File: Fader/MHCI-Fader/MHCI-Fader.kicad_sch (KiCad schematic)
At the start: 29 parts, among them J1 Conn_01x06, SW1 SW_Push_LED, U1 TJA1051T, U3 SRV05-4

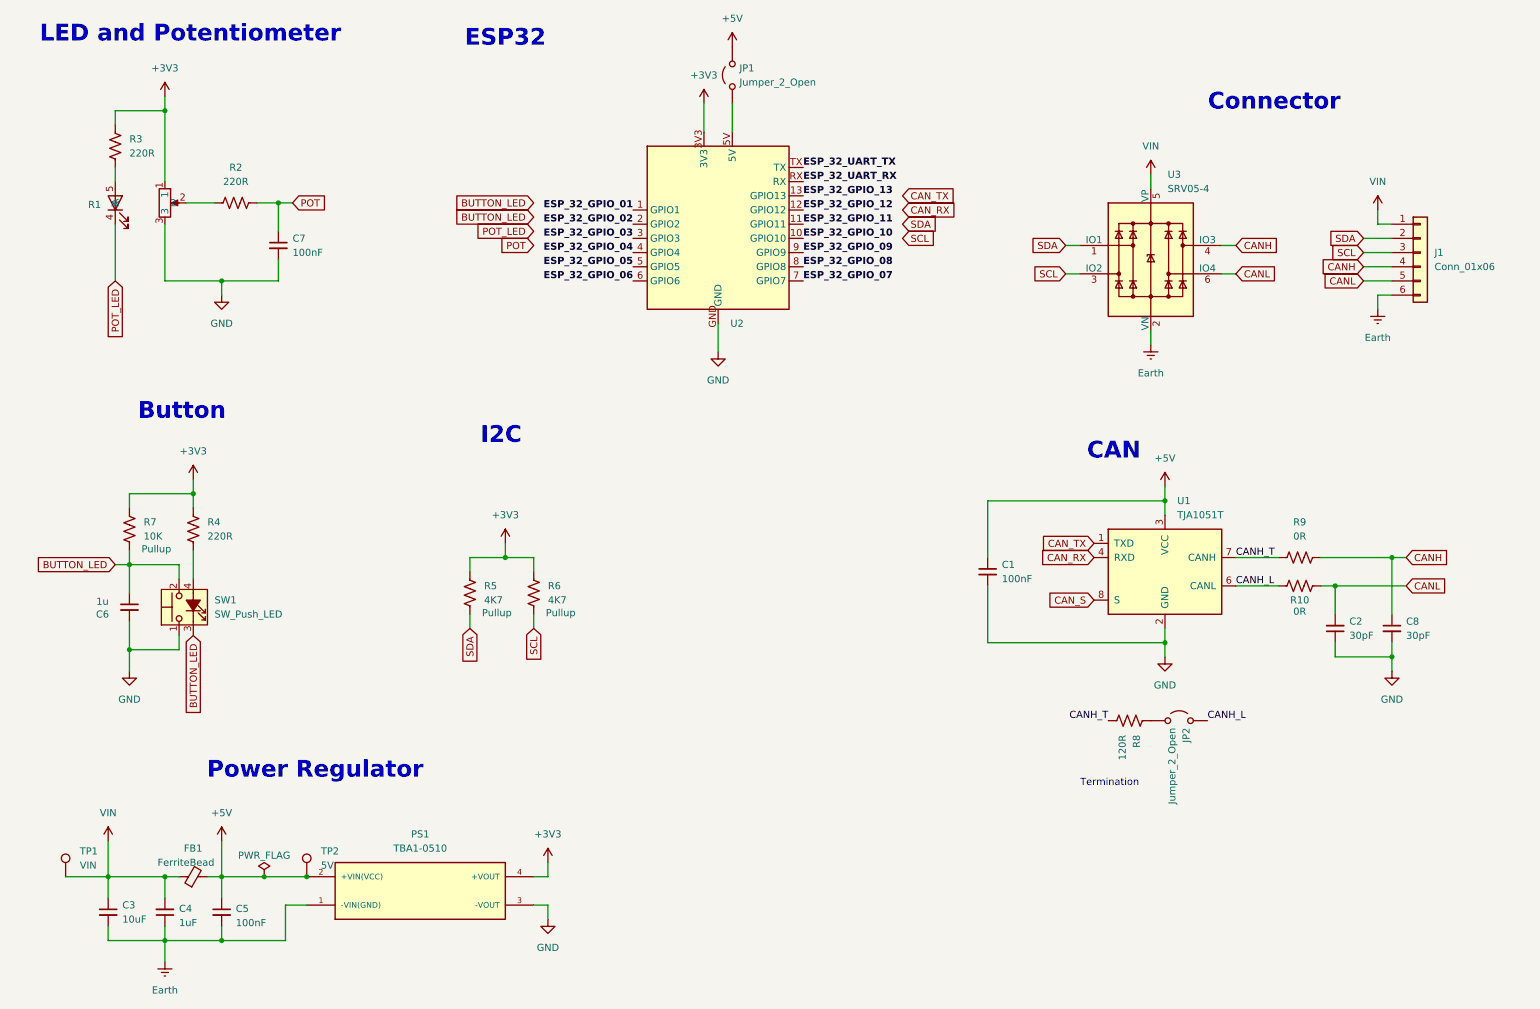
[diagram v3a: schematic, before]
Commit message: Fader layout complete
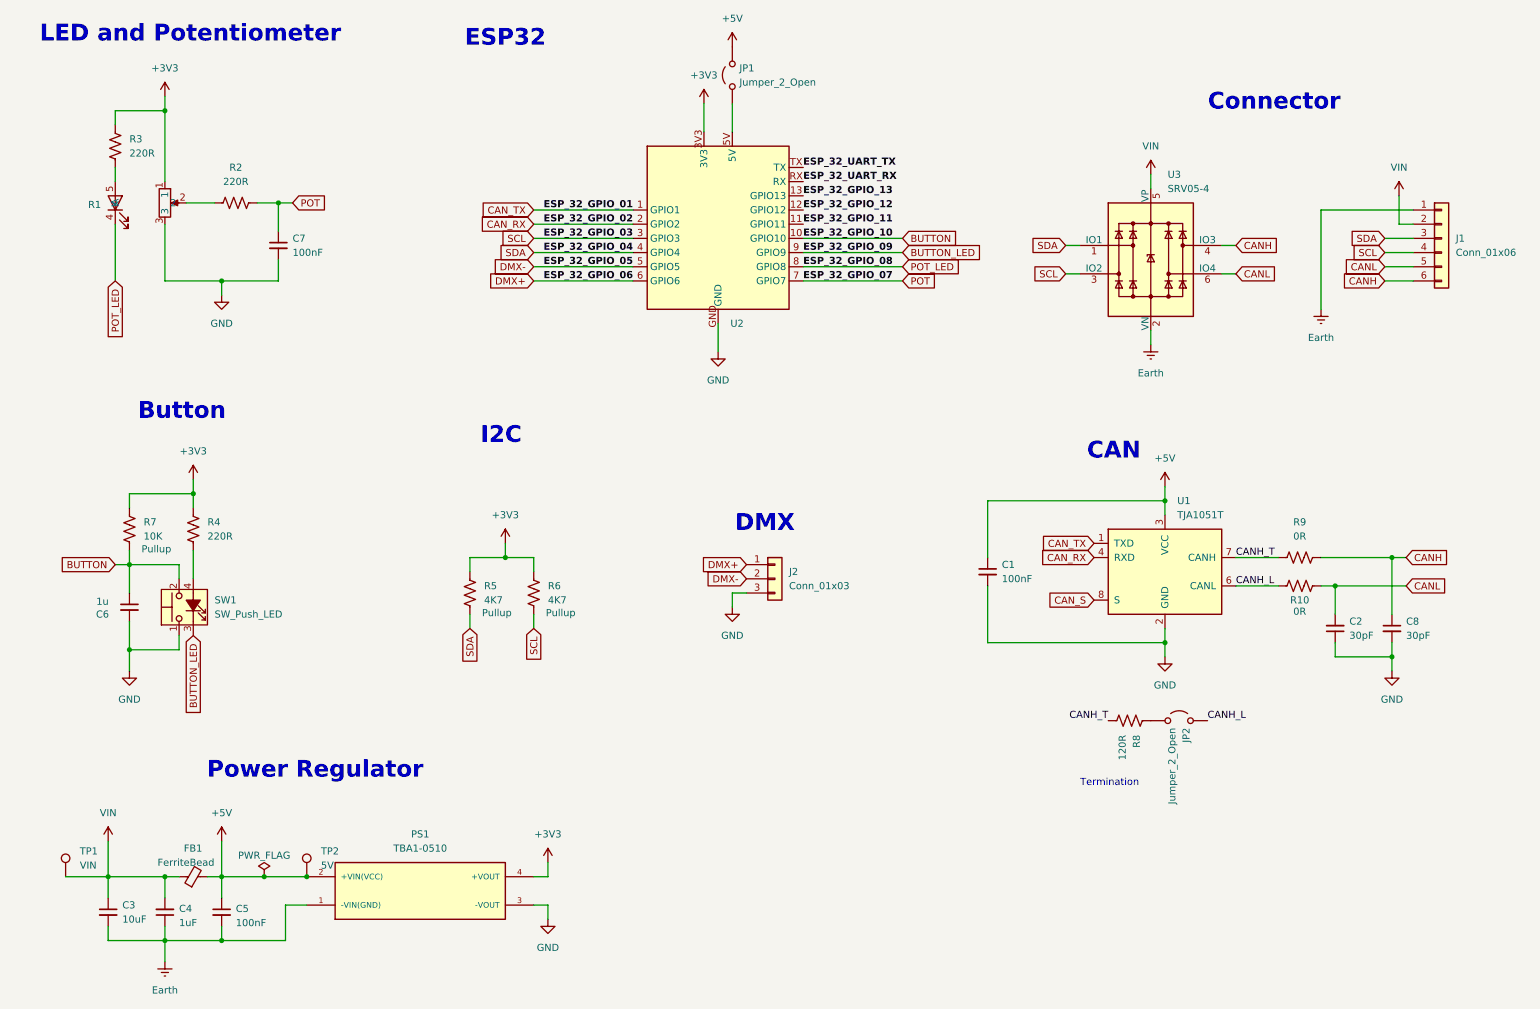
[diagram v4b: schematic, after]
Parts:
- added J2: Conn_01x03, Connector_PinHeader_2.54mm:PinHeader_1x03_P2.54mm_Vertical, symbol Connector_Generic:Conn_01x03
- R1: footprint FaderLibrary:Linear Potentiometer LED 100mm -> FaderLibrary:Linear Potentiometer LED 60mm
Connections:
- net ESP_32_GPIO_01 is gone; now on net CAN_TX: U2.1 (GPIO1)
- net ESP_32_GPIO_02 is gone; now on net CAN_RX: U2.2 (GPIO2)
- net ESP_32_GPIO_03 is gone; now on net SCL: U2.3 (GPIO3)
- net ESP_32_GPIO_04 is gone; now on net SDA: U2.4 (GPIO4)
- net ESP_32_GPIO_07 is gone; now on net POT: U2.7 (GPIO7)
- net ESP_32_GPIO_08 is gone; now on net POT_LED: U2.8 (GPIO8)
- net ESP_32_GPIO_09 is gone; now on net BUTTON_LED: U2.9 (GPIO9)
- net BUTTON_LED: no longer C6.1, R7.2, SW1.2
- net CANH: now also J1.6 (Pin_6); no longer J1.4 (Pin_4)
- net Earth: now also J1.1 (Pin_1); no longer J1.6 (Pin_6)
- net GND: now also J2.3 (Pin_3)
- net SCL: now also J1.4 (Pin_4); no longer J1.3 (Pin_3)
- net SDA: now also J1.3 (Pin_3); no longer J1.2 (Pin_2)
- net VIN: now also J1.2 (Pin_2); no longer J1.1 (Pin_1)
- net ESP_32_GPIO_05 renamed DMX-
- net DMX-: now also J2.2 (Pin_2)
- net ESP_32_GPIO_06 renamed DMX+
- net DMX+: now also J2.1 (Pin_1)
- net ESP_32_GPIO_10 renamed BUTTON
- net BUTTON: now also C6.1, R7.2, SW1.2
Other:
- note added: "DMX"

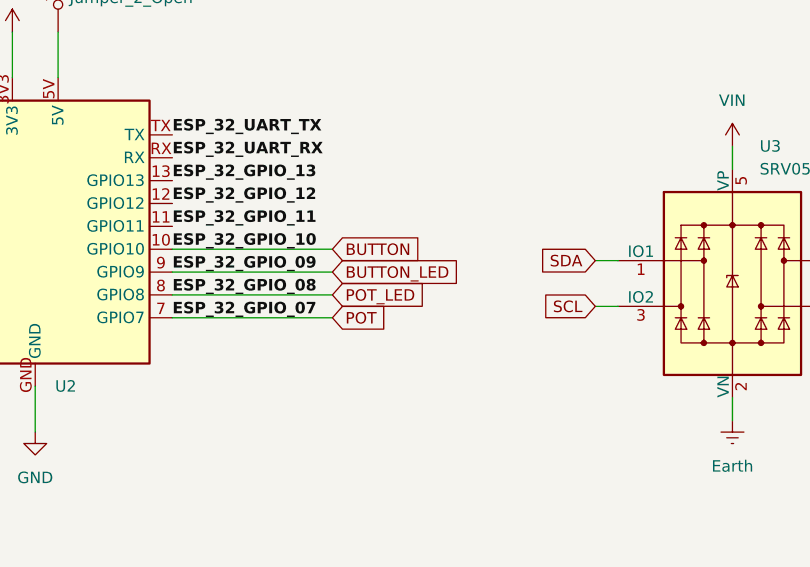
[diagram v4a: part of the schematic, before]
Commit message: Adjusted fader layout to compact arrangement
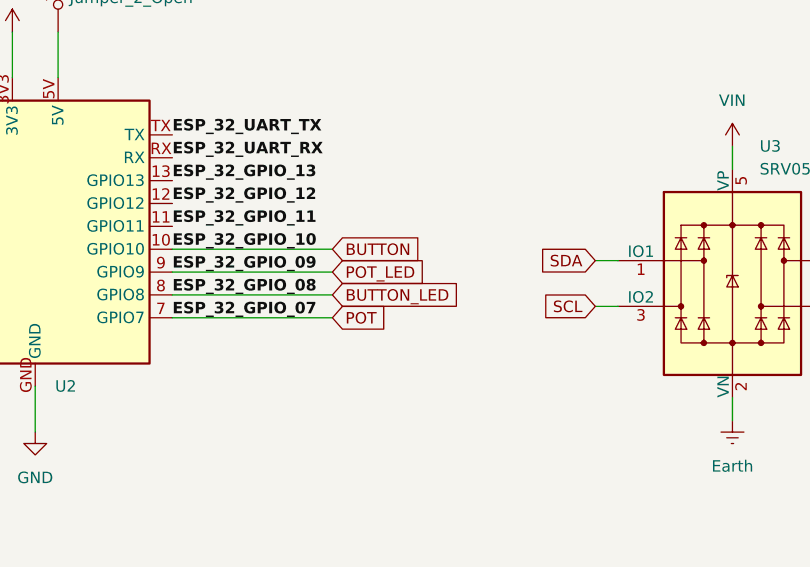
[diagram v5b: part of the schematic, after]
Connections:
- net BUTTON_LED: now also U2.8 (GPIO8); no longer U2.9 (GPIO9)
- net POT_LED: now also U2.9 (GPIO9); no longer U2.8 (GPIO8)
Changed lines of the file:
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@@
+		)
+	)
+	(global_label "BUTTON_LED"
+		(shape input)
+		(at 175.26 60.96 0)
+		(fields_autoplaced yes)
+		(effects
+			(font
+				(size 1.27 1.27)
+			)
+			(justify left)
+		)
+		(property "Intersheetrefs" "${INTERSHEET_REFS}"
+			(at 189.8566 60.96 0)
+			(effects
+				(font
+					(size 1.27 1.27)
+				)
+				(justify left)
+				(hide yes)
+			)
 		)
 	)
@@
 	(global_label "POT_LED"
 		(shape input)
-		(at 175.26 60.96 0)
-		(fields_autoplaced yes)
-		(effects
-			(font
-				(size 1.27 1.27)
-			)
-			(justify left)
-		)
-		(property "Intersheetrefs" "${INTERSHEET_REFS}"
-			(at 186.228 60.96 0)
+		(at 175.26 58.42 0)
+		(fields_autoplaced yes)
+		(effects
+			(font
+				(size 1.27 1.27)
+			)
+			(justify left)
+		)
+		(property "Intersheetrefs" "${INTERSHEET_REFS}"
+			(at 186.228 58.42 0)
 			(effects
 				(font
@@
 				(hide yes)
 			)
-		)
-	)
-	(global_label "BUTTON_LED"
-		(shape input)
-		(at 175.26 58.42 0)
-		(fields_autoplaced yes)
-		(effects
-			(font
-				(size 1.27 1.27)
-			)
-			(justify left)
-		)
-		(property "Intersheetrefs" "${INTERSHEET_REFS}"
-			(at 189.8566 58.42 0)
-			(effects
-				(font
-					(size 1.27 1.27)
-				)
-				(justify left)
-				(hide yes)
-			)

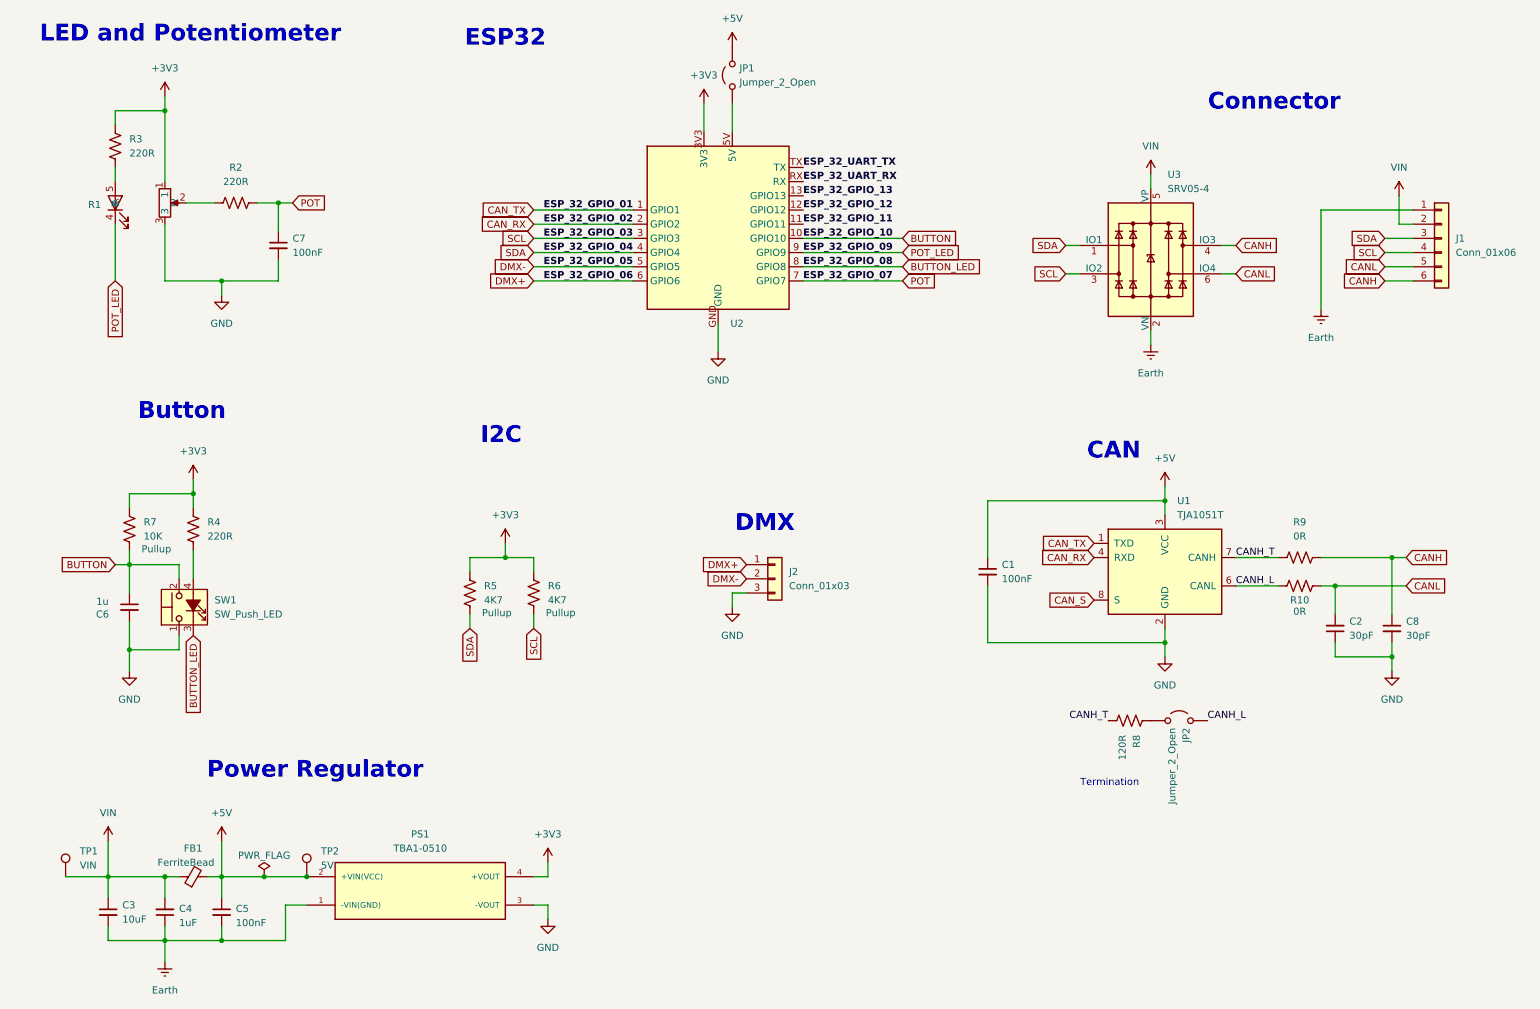
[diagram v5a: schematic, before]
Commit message: MHCI Fader - Add logic level converter and re-route traces
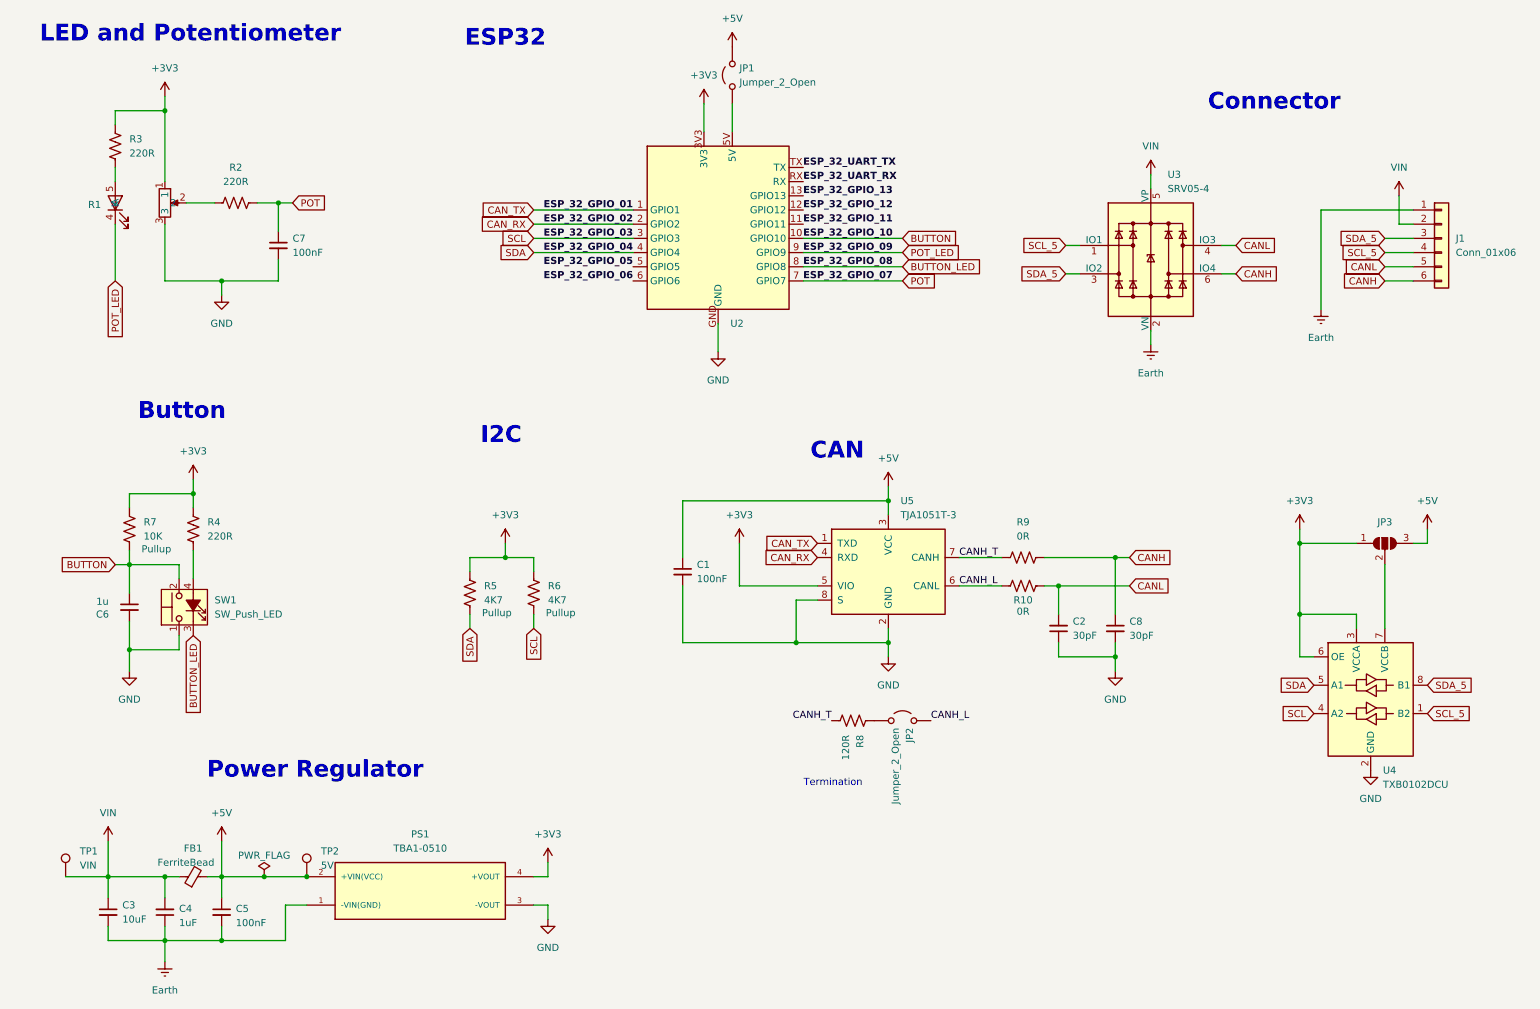
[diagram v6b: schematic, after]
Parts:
- removed J2: Conn_01x03, Connector_PinHeader_2.54mm:PinHeader_1x03_P2.54mm_Vertical, symbol Connector_Generic:Conn_01x03
- removed U1: TJA1051T, Package_SO:SOIC-8_3.9x4.9mm_P1.27mm, symbol Interface_CAN_LIN:TJA1051T
- added JP3: SolderJumper_3_Open, Jumper:SolderJumper-3_P1.3mm_Open_RoundedPad1.0x1.5mm, symbol Jumper:SolderJumper_3_Open
- added U4: TXB0102DCU, Package_SO:VSSOP-8_2.3x2mm_P0.5mm, symbol Logic_LevelTranslator:TXB0102DCU
- added U5: TJA1051T-3, Package_SO:SOIC-8_3.9x4.9mm_P1.27mm, symbol Interface_CAN_LIN:TJA1051T-3
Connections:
- net +3V3: now also JP3.1 (A), U4.3 (VCCA), U4.6 (OE), U5.5 (VIO)
- net +5V: now also JP3.3 (B), U5.3 (VCC)
- net CANH: now also U3.6 (IO4); no longer U3.4 (IO3)
- net CANH_L: now also U5.6 (CANL)
- net CANH_T: now also U5.7 (CANH)
- net CANL: now also U3.4 (IO3); no longer U3.6 (IO4)
- net CAN_RX: now also U5.4 (RXD)
- net CAN_TX: now also U5.1 (TXD)
- net GND: now also U4.2 (GND), U5.2 (GND), U5.8 (S)
- net SCL: now also U4.4 (A2); no longer J1.4 (Pin_4), U3.3 (IO2)
- net SDA: now also U4.5 (A1); no longer J1.3 (Pin_3), U3.1 (IO1)
- net DMX+ renamed ESP_32_GPIO_06
- net DMX- renamed ESP_32_GPIO_05
- new net: JP3.2 (C), U4.7 (VCCB)
- new net SCL_5: J1.4 (Pin_4), U3.1 (IO1), U4.1 (B2)
- new net SDA_5: J1.3 (Pin_3), U3.3 (IO2), U4.8 (B1)
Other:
- note removed: "DMX"
- moved on the sheet: C1, C2, C8, JP2, R10, R8, R9
